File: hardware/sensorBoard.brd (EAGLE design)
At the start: 113.9 x 40 mm, 35 parts, among them IC1 LM35CZ

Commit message: wired amplifier and start to set up SPI for ADC in schematic
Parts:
- removed R1, R13, R14, R15, R2, R3, R4, R5, R6: 1000, eagle-ltspice:0207/10
- removed SV8: (no value), con-lstb:MA13-1
- added SV2: (no value), con-lstb:MA06-1
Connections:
- net N$10 renamed REF1
- removed net N$14: R1.2, R2.1
- removed net N$9: R18.2
- new net MISO: SV2.6
- new net MOSI: SV2.5
- new net N$1: U$4.8
- new net N$16: U$4.2
- new net N$18: U$4.3
- new net N$19: U$2.1
- new net N$24: U$2.8
- new net N$26: U$3.1
- new net N$27: U$3.8
- new net N$28: U$3.2
- new net N$29: U$3.3
- new net N$4: U$1.3
- new net NSS: SV2.4
- new net REF0: R16.2, R18.2
- new net SCLK: SV2.3
- new net SENSOR_1_OUT: U$4.6
- new net SENSOR_2_OUT: U$1.6
- new net SENSOR_3_OUT: U$2.6
- new net SENSOR_4_OUT: U$3.6
- net GND: now also SV2.1, U$1.4, U$1.5, U$2.4, U$2.5, U$3.4, U$3.5, U$4.4, U$4.5; no longer SV8.12
- net N$12: now also U$2.2; no longer R13.1, R14.2
- net N$13: now also U$2.3; no longer R4.1, R5.2
- net N$2: now also U$4.1; no longer R15.2
- net N$3: now also U$1.2; no longer R6.1
- net N$5: now also U$1.1; no longer R1.1, R3.1
- net N$7: now also U$1.8; no longer R2.2, R3.2
- net OUT_S1_+: no longer SV8.1
- net OUT_S1_-: no longer SV8.2
- net OUT_S2_+: no longer SV8.3
- net OUT_S2_-: no longer SV8.4
- net OUT_S3_+: no longer SV8.5
- net OUT_S3_-: no longer SV8.6
- net OUT_S4_+: no longer SV8.7
- net OUT_S4_-: no longer SV8.8
- net OUT_S_TEMP: no longer SV8.9
- net VCC: now also SV2.2, U$1.7, U$2.7, U$3.7, U$4.7; no longer SV8.13

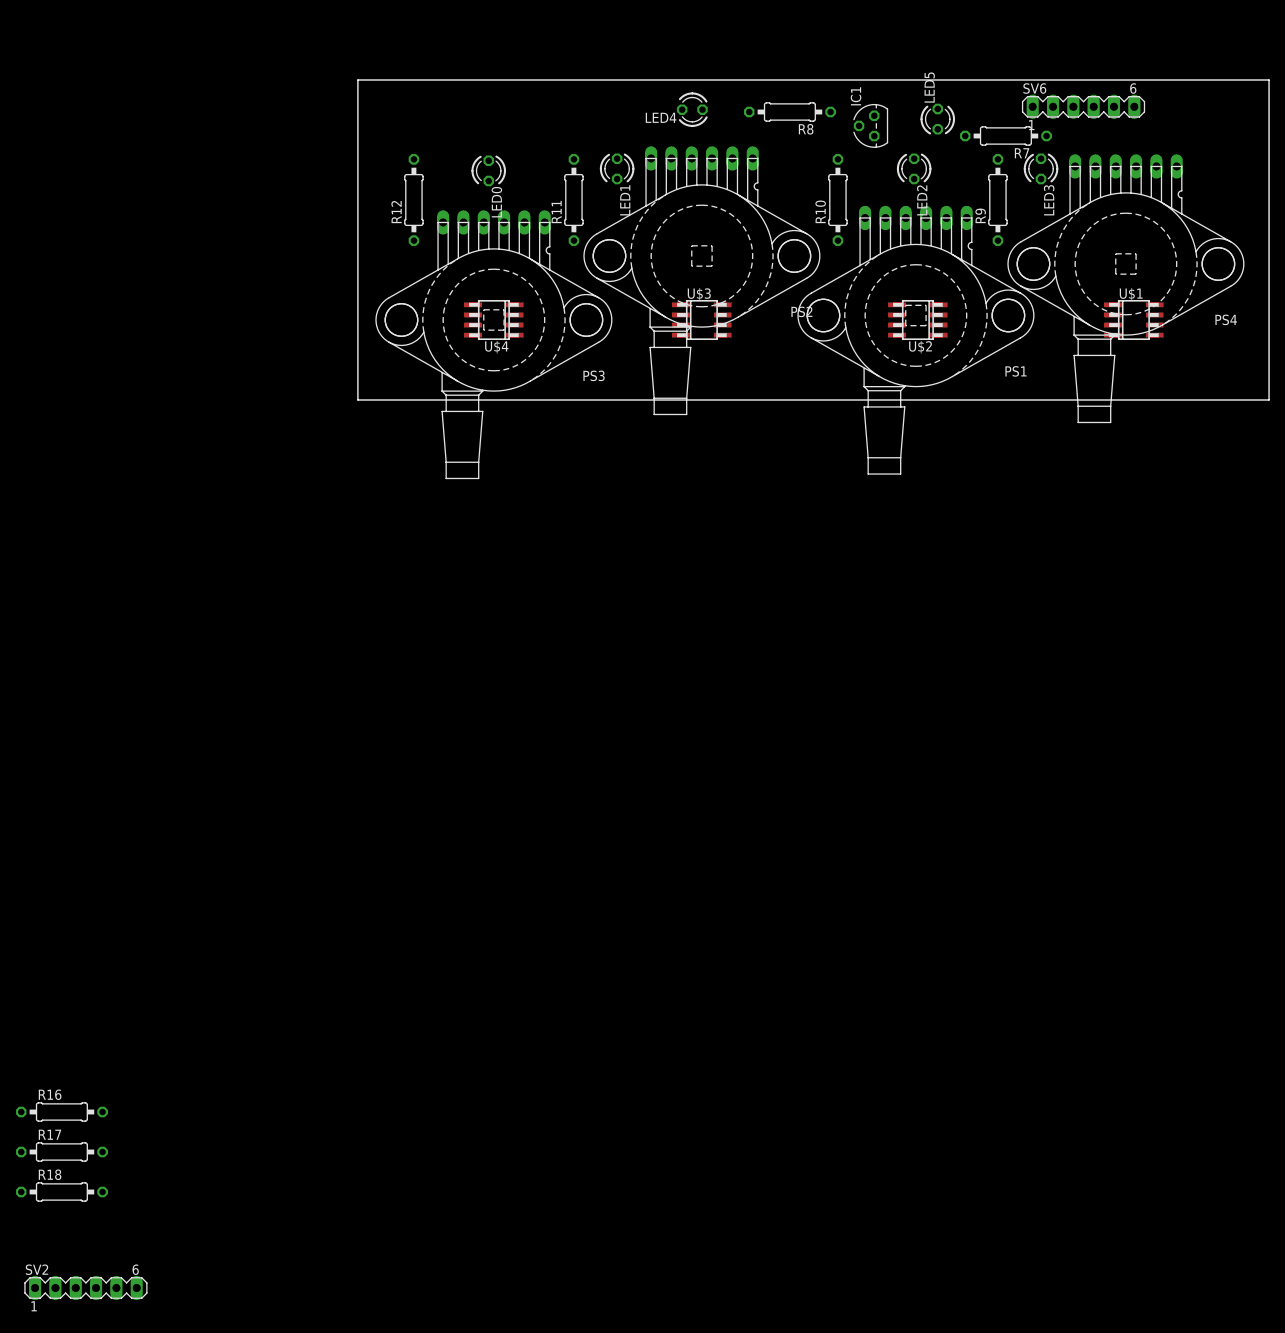
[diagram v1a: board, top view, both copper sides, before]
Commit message: build sensor sandwich board to get it smaller. Still waiting for the ADC we would like to use
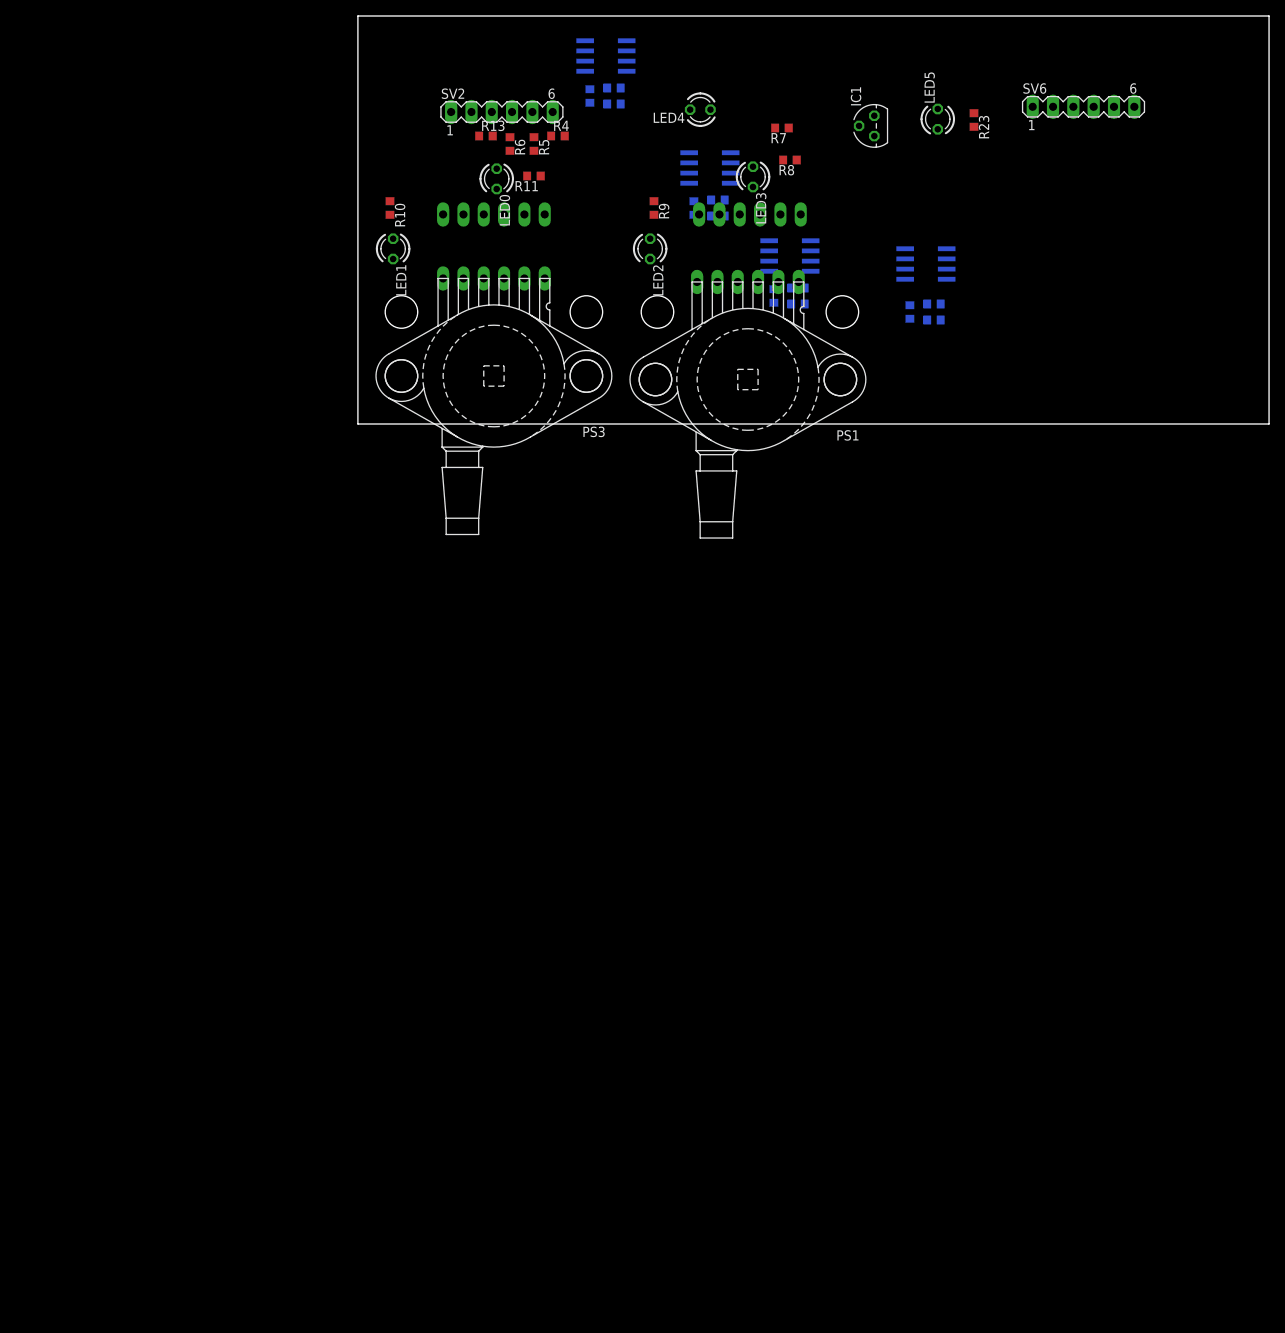
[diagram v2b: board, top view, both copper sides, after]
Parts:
- removed R12: 100, eagle-ltspice:0207/10
- added R1, R14, R15, R19, R2, R20, R21, R22, R3: 1000, rcl:R0603
- added R13, R4, R5, R6: 100k, rcl:R0603
- added R23: 100, rcl:R0603
- R10, R11, R16, R17, R18, R7, R8, R9: device eagle-ltspice:0207/10 -> rcl:R0603
- moved SV2 155.9 mm to (17.0, 36.0)
- moved R18 146.2 mm to (41.0, 24.0), flipped to the bottom, turned to 270 degrees
- moved R17 144.5 mm to (44.0, 25.0), flipped to the bottom, turned to 180 degrees
- moved R16 136.6 mm to (54.0, 12.0), flipped to the bottom, turned to 180 degrees
- moved R10 56.0 mm to (3.00, 24.0), turned to 270 degrees
- moved U$4 54.5 mm to (70.0, 17.0), flipped to the bottom
- moved PS4 47.4 mm to (48.0, 11.0), flipped to the bottom
- moved U$1 43.7 mm to (53.0, 18.0), flipped to the bottom, turned to 90 degrees
- moved R9 43.0 mm to (36.0, 24.0), turned to 270 degrees
- moved LED3 36.0 mm to (48.4, 27.9)
- moved U$3 35.1 mm to (30.0, 43.0), flipped to the bottom, turned to 90 degrees
- moved LED2 34.5 mm to (35.5, 18.9)
- moved U$2 32.2 mm to (43.0, 29.0), flipped to the bottom
- moved LED1 29.7 mm to (3.40, 18.9)
- moved R7 28.0 mm to (52.0, 34.0)
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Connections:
- removed net REF0: R16.2, R18.2
- removed net REF1: R17.1, R18.1
- new net N$10: R14.1, R16.1
- new net N$30: R17.2, R18.1
- new net N$35: R20.2, R21.1
- new net N$8: R1.2, R2.1
- net LED0: now also R11.1; no longer R12.1
- net LED1: now also R10.1; no longer R11.1
- net LED2: now also R9.1; no longer R10.1
- net LED3: now also R8.1; no longer R9.1
- net LED4: now also R7.1; no longer R8.1
- net LED5: now also R23.1; no longer R7.1
- net MISO: now also R4.1, R4.2
- net MOSI: now also R5.1, R5.2
- net N$1: now also R2.2, R3.2
- net N$11: now also R14.2, R15.1; no longer R16.1, R17.2
- net N$17: now also R7.2; no longer R8.2
- net N$19: now also R17.1, R19.1
- net N$2: now also R1.1, R3.1
- net N$20: now also R8.2; no longer R9.2
- net N$21: now also R9.2; no longer R10.2
- net N$22: now also R10.2; no longer R11.2
- net N$23: now also R11.2; no longer R12.2
- net N$24: now also R18.2, R19.2
- net N$26: now also R20.1, R22.1
- net N$27: now also R21.2, R22.2
- net N$6: now also R23.2; no longer R7.2
- net N$7: now also R15.2, R16.2
- net NSS: now also R6.1, R6.2
- net SCLK: now also R13.1, R13.2
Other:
- board size 113.9 x 40 mm -> 113.9 x 51 mm
